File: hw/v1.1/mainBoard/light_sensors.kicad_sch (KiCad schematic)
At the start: 6 parts, among them U4 VEML7700, U6 ML8511

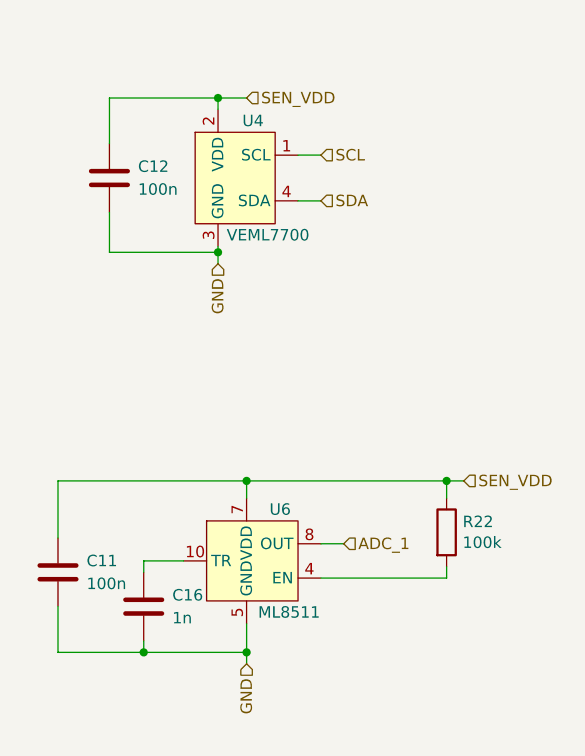
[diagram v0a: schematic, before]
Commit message: Beautify schematics in KiCad
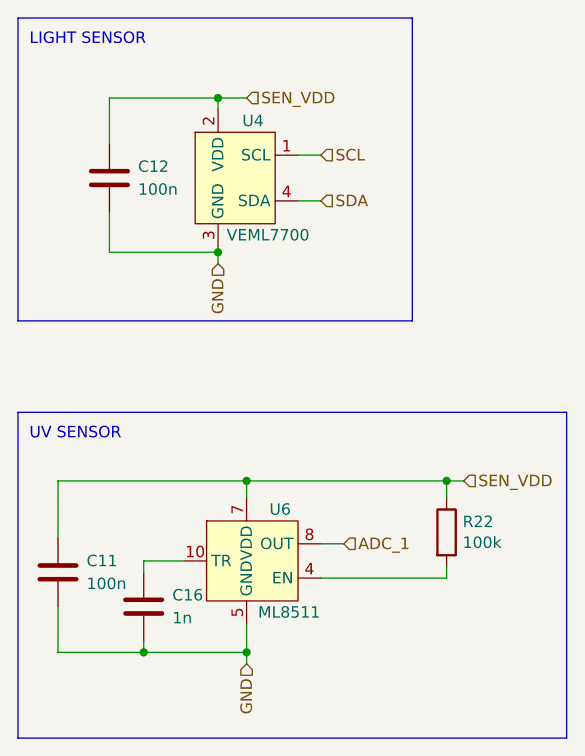
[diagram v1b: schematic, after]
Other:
- note added: "LIGHT SENSOR"
- note added: "UV SENSOR"
- company: (none) -> Martin Kousal
- title: (none) -> iotAirMonitoring
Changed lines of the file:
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@@
   (paper "A4")
   (title_block
+    (title "iotAirMonitoring")
     (date "2022-05-09")
     (rev "v1.1")
+    (company "Martin Kousal")
   )
   (junction (at 121.92 52.07) (diameter 0) (color 0 0 0 0)
@@
   (junction (at 113.665 113.665) (diameter 0) (color 0 0 0 0)
   )
+  (polyline (pts (xy 143.51 76.835) (xy 99.695 76.835))
+    (stroke (width 0) (type default) (color 0 0 0 0))
+  )
   (wire (pts (xy 104.14 100.965) (xy 104.14 94.615))
+    (stroke (width 0) (type default) (color 0 0 0 0))
+  )
+  (polyline (pts (xy 99.695 43.18) (xy 143.51 43.18))
+    (stroke (width 0) (type default) (color 0 0 0 0))
+  )
+  (polyline (pts (xy 99.695 86.995) (xy 160.655 86.995))
     (stroke (width 0) (type default) (color 0 0 0 0))
   )
@@
     (stroke (width 0) (type default) (color 0 0 0 0))
   )
+  (polyline (pts (xy 99.695 43.18) (xy 99.695 76.835))
+    (stroke (width 0) (type default) (color 0 0 0 0))
+  )
   (wire (pts (xy 130.81 63.5) (xy 133.35 63.5))
     (stroke (width 0) (type default) (color 0 0 0 0))
@@
     (stroke (width 0) (type default) (color 0 0 0 0))
   )
+  (polyline (pts (xy 143.51 43.18) (xy 143.51 76.835))
+    (stroke (width 0) (type default) (color 0 0 0 0))
+  )
   (wire (pts (xy 104.14 108.585) (xy 104.14 113.665))
     (stroke (width 0) (type default) (color 0 0 0 0))
@@
     (stroke (width 0) (type default) (color 0 0 0 0))
   )
+  (polyline (pts (xy 160.655 123.19) (xy 99.695 123.19))
+    (stroke (width 0) (type default) (color 0 0 0 0))
+  )
   (wire (pts (xy 133.35 105.41) (xy 147.32 105.41))
+    (stroke (width 0) (type default) (color 0 0 0 0))
+  )
+  (polyline (pts (xy 160.655 86.995) (xy 160.655 123.19))
     (stroke (width 0) (type default) (color 0 0 0 0))
   )
@@
     (stroke (width 0) (type default) (color 0 0 0 0))
   )
+  (polyline (pts (xy 99.695 86.995) (xy 99.695 123.19))
+    (stroke (width 0) (type default) (color 0 0 0 0))
+  )
   (wire (pts (xy 125.095 113.665) (xy 125.095 114.935))
     (stroke (width 0) (type default) (color 0 0 0 0))
@@
     (stroke (width 0) (type default) (color 0 0 0 0))
   )
+  (text "LIGHT SENSOR" (at 100.965 46.355 0)
+    (effects (font (size 1.27 1.27)) (justify left bottom))
+  )
+  (text "UV SENSOR" (at 100.965 90.17 0)
+    (effects (font (size 1.27 1.27)) (justify left bottom))
+  )
   (hierarchical_label "GND" (shape input) (at 121.92 70.485 270)
